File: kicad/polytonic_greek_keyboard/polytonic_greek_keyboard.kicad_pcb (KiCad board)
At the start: 2 copper layers, 10 parts, among them SW1 SW_Wuerth_450301014042, SW2 RotaryEncoder_Switch_MP, SW3 SW_SPST, SW4 SW_SP4T_NR01104, U1 ESP32-S2-WROVER

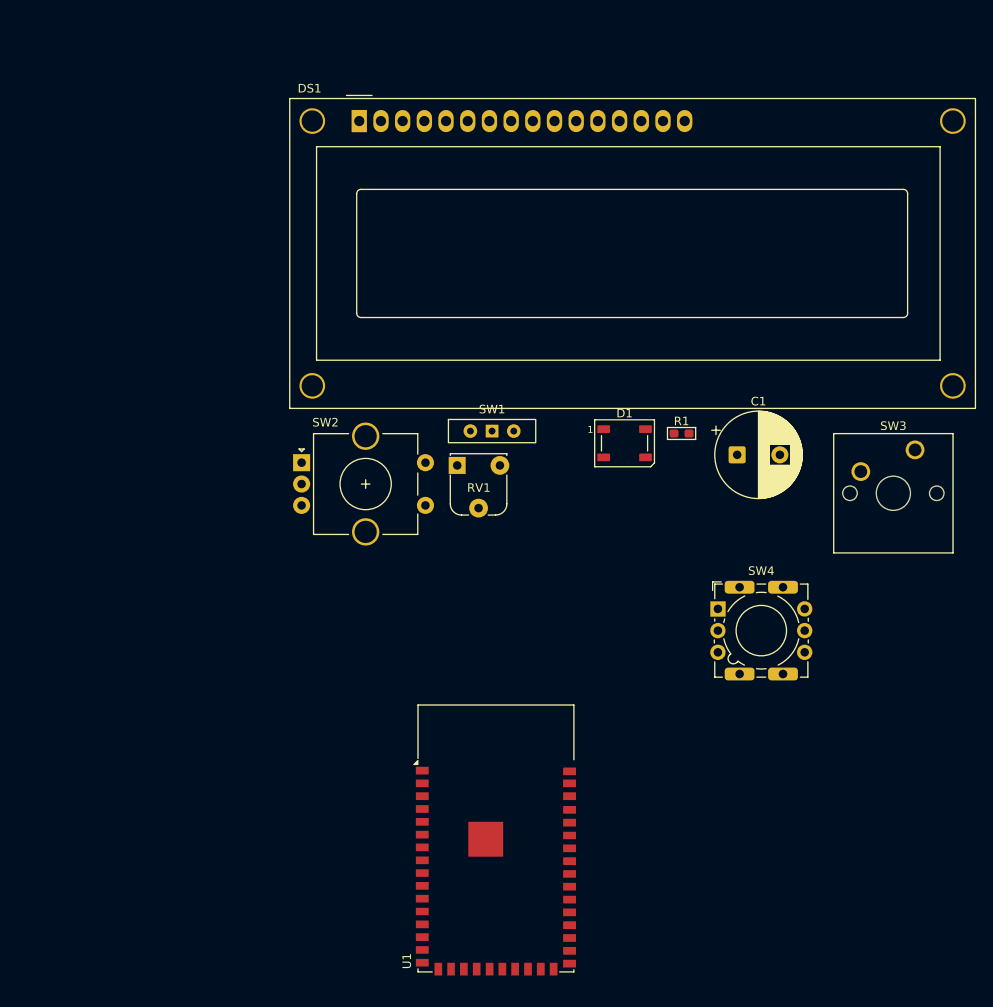
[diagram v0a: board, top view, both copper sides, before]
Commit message: [ADD] the kicad desing of the I²C chip for the keybard
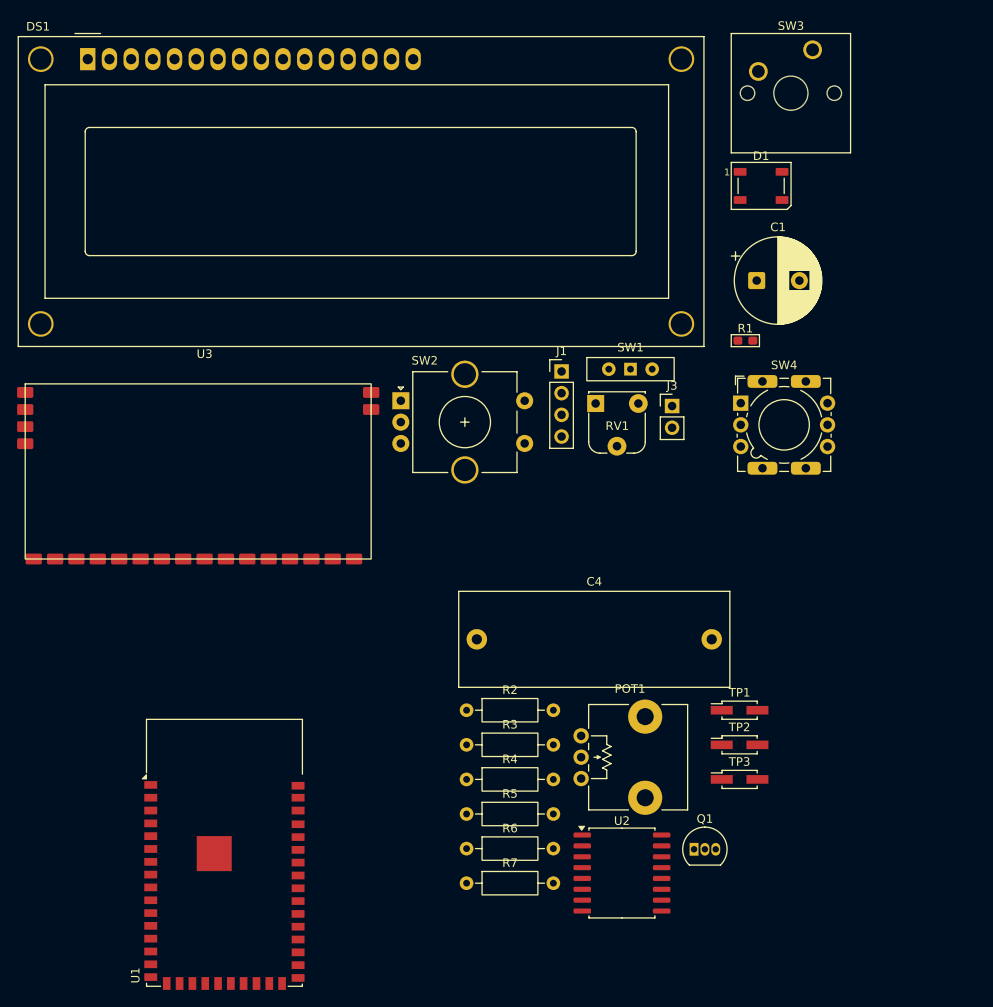
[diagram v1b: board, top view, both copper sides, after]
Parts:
- added C4: 0.1uF, Capacitor_THT:C_Rect_L31.5mm_W11.0mm_P27.50mm_MKS4, F.Cu at (85.2, 94.6)
- added J1: PINHD_1x4_Male, Connector_PinHeader_2.54mm:PinHeader_1x04_P2.54mm_Vertical, F.Cu at (95.1, 63.2)
- added J3: PINHD_1x2_Male, Connector_PinHeader_2.54mm:PinHeader_1x02_P2.54mm_Vertical, F.Cu at (108.0, 67.3)
- added POT1: 16mm_CtrDet_10k, PCM_Potentiometer_THT_US_AKL:Potentiometer_Alps_RK09L_Single_Vertical, F.Cu at (97.4, 110.9)
- added Q1: S8050, Package_TO_SOT_THT:TO-92_Inline, F.Cu at (110.6, 119.2)
- added R2: 47k, Resistor_THT:R_Axial_DIN0207_L6.3mm_D2.5mm_P10.16mm_Horizontal, F.Cu at (84.0, 102.9)
- added R3: 1k, Resistor_THT:R_Axial_DIN0207_L6.3mm_D2.5mm_P10.16mm_Horizontal, F.Cu at (84.0, 107.0)
- added R4: 1k, Resistor_THT:R_Axial_DIN0207_L6.3mm_D2.5mm_P10.16mm_Horizontal, F.Cu at (84.0, 111.0)
- added R5: 1k, Resistor_THT:R_Axial_DIN0207_L6.3mm_D2.5mm_P10.16mm_Horizontal, F.Cu at (84.0, 115.0)
- added R6: 47k, Resistor_THT:R_Axial_DIN0207_L6.3mm_D2.5mm_P10.16mm_Horizontal, F.Cu at (84.0, 119.1)
- added R7: 47k, Resistor_THT:R_Axial_DIN0207_L6.3mm_D2.5mm_P10.16mm_Horizontal, F.Cu at (84.0, 123.2)
- added TP1: TestPoint_2Pole, Pin_Headers:Pin_Header_Straight_2x01_Pitch2.00mm_SMD, F.Cu at (115.9, 102.9)
- added TP2: TestPoint_2Pole, Pin_Headers:Pin_Header_Straight_2x01_Pitch2.00mm_SMD, F.Cu at (115.9, 107.0)
- added TP3: TestPoint_2Pole, Pin_Headers:Pin_Header_Straight_2x01_Pitch2.00mm_SMD, F.Cu at (115.9, 111.0)
- added U2: PCF8574T, Package_SO:SOIC-16W_7.5x10.3mm_P1.27mm, F.Cu at (102.1, 122.0)
- added U3: ~, polytonic_greek_keyboard:I²C, F.Cu at (53.3, 61.7)
- moved SW3 48.4 mm to (124.5, 25.6)
- moved D1 34.1 mm to (118.4, 41.5)
- moved DS1 32.6 mm to (39.6, 26.7)
- moved U1 31.8 mm to (55.6, 123.4)
- moved SW4 24.2 mm to (116.1, 67.0)
- moved C1 20.5 mm to (117.9, 52.6)
- moved RV1 17.8 mm to (101.6, 69.0)
- moved SW1 17.8 mm to (103.1, 63.0)
- moved SW2 13.7 mm to (76.3, 66.7)
- moved R1 13.2 mm to (116.6, 59.6)
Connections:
- net /display/VDD_SCREEN renamed /display/VCC_SCREEN
- DS1 pad 1: VSS -> Net-(DS1-VSS)
- DS1 pad 11: unconnected-(DS1-D4-Pad11) -> Net-(DS1-D4)
- DS1 pad 12: unconnected-(DS1-D5-Pad12) -> Net-(DS1-D5)
- DS1 pad 13: unconnected-(DS1-D6-Pad13) -> Net-(DS1-D6)
- DS1 pad 14: unconnected-(DS1-D7-Pad14) -> Net-(DS1-D7)
- DS1 pad 16: GND -> Net-(DS1-LED(-))
- DS1 pad 3: unconnected-(DS1-VO-Pad3) -> Net-(DS1-VO)
- DS1 pad 4: unconnected-(DS1-RS-Pad4) -> Net-(DS1-RS)
- DS1 pad 5: unconnected-(DS1-R/W-Pad5) -> Net-(DS1-R/W)
- DS1 pad 6: unconnected-(DS1-E-Pad6) -> Net-(DS1-E)
- RV1 pad 1: Net-(DS1-LED(+)) -> Net-(U3-LED_VCC)
- RV1 pad 3: Net-(DS1-VDD) -> Net-(SW1-C)
- SW1 pad 2: Net-(DS1-VDD) -> Net-(SW1-C)

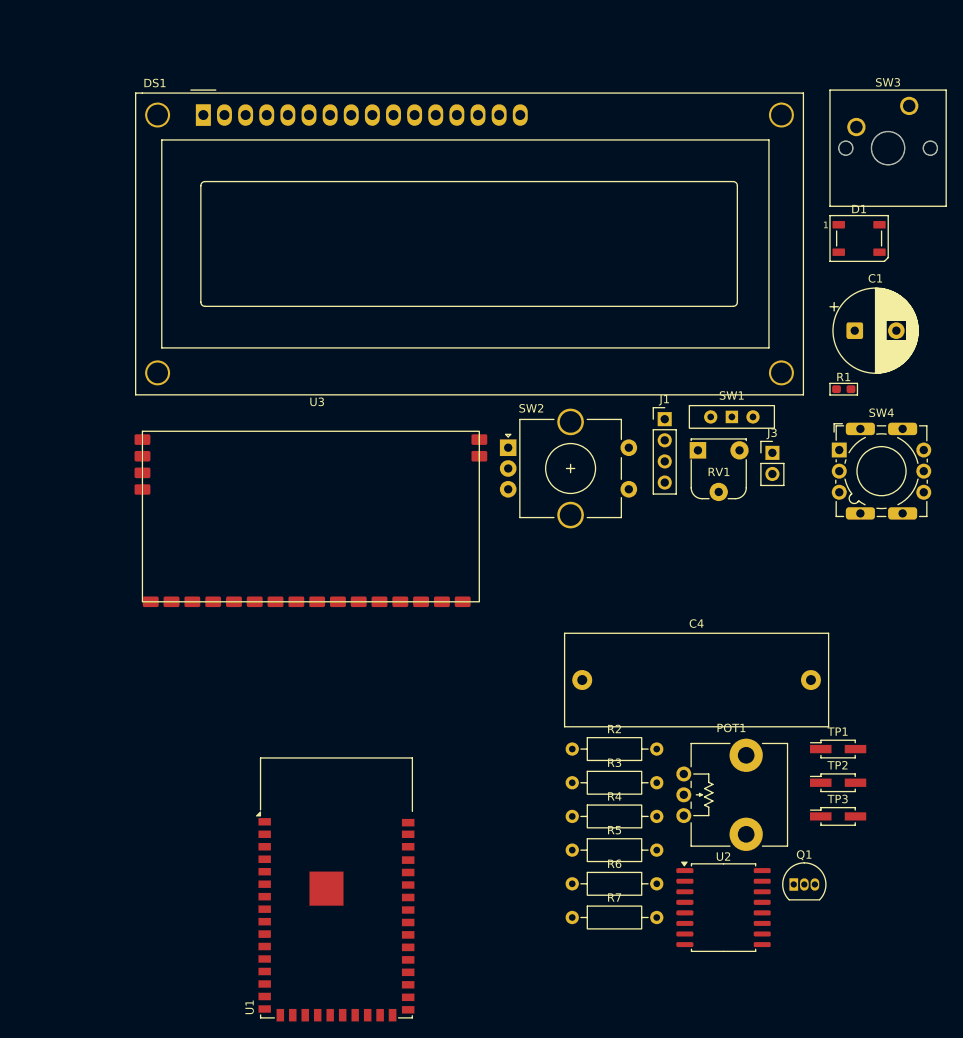
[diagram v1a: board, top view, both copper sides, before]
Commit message: [ADD] an initial matrix of what the keyboard will look like logically
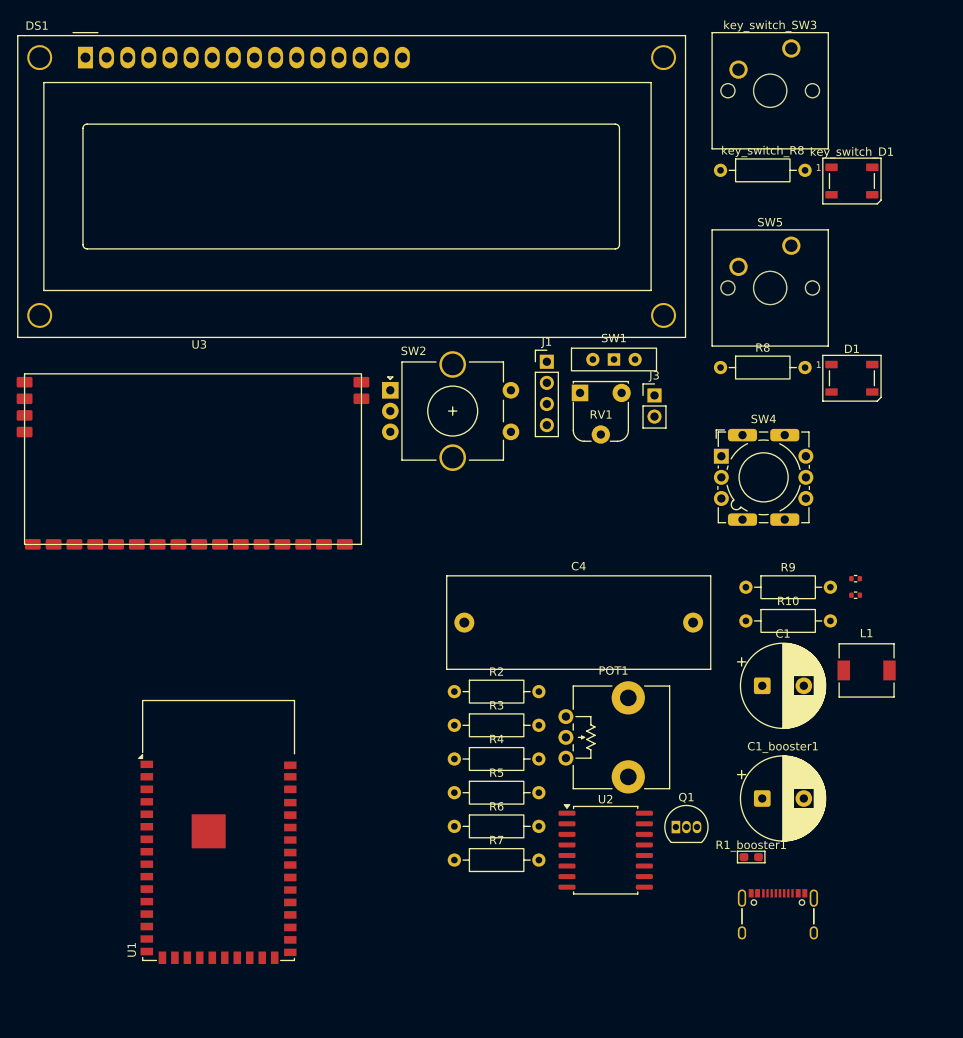
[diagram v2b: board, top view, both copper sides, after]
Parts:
- removed R1: 330R_0603, PCM_Resistor_SMD_AKL:R_0603_1608Metric_Pad1.05x0.95mm_HandSolder
- removed SW3: SW_SPST, Button_Switch_Keyboard:SW_Cherry_MX_1.00u_PCB
- removed TP1, TP2, TP3: TestPoint_2Pole, Pin_Headers:Pin_Header_Straight_2x01_Pitch2.00mm_SMD
- added C1_booster1: 1000uF_16V, Capacitor_THT:CP_Radial_D10.0mm_P5.00mm, F.Cu at (106.8, 108.8)
- added J2: USB_C_Receptacle, PCM_SparkFun-Connector:USB-C_16, F.Cu at (108.7, 119.9)
- added L1: FerriteBead_0603_1.5A, Inductor_SMD:L_6.3x6.3_H3, F.Cu at (119.3, 93.4)
- added R10: 22ohm, Resistor_THT:R_Axial_DIN0207_L6.3mm_D2.5mm_P10.16mm_Horizontal, F.Cu at (104.8, 87.5)
- added R11: 5.1k, PCM_SparkFun-Resistor:R_0402_1005Metric, F.Cu at (118.0, 82.4)
- added R12: 5.1k, PCM_SparkFun-Resistor:R_0402_1005Metric, F.Cu at (118.0, 84.4)
- added R1_booster1: 330R_0603, PCM_Resistor_SMD_AKL:R_0603_1608Metric_Pad1.05x0.95mm_HandSolder, F.Cu at (105.5, 115.9)
- added R8: 330ohm, Resistor_THT:R_Axial_DIN0207_L6.3mm_D2.5mm_P10.16mm_Horizontal, F.Cu at (101.8, 57.0)
- added R9: 22ohm, Resistor_THT:R_Axial_DIN0207_L6.3mm_D2.5mm_P10.16mm_Horizontal, F.Cu at (104.8, 83.4)
- added SW5: SW_SPST, Button_Switch_Keyboard:SW_Cherry_MX_1.00u_PCB, F.Cu at (110.3, 42.4)
- added key_switch_D1: WS2812B, LED_SMD:LED_WS2812B_PLCC4_5.0x5.0mm_P3.2mm, F.Cu at (117.6, 34.6)
- added key_switch_R8: 330ohm, Resistor_THT:R_Axial_DIN0207_L6.3mm_D2.5mm_P10.16mm_Horizontal, F.Cu at (101.8, 33.3)
- added key_switch_SW3: SW_SPST, Button_Switch_Keyboard:SW_Cherry_MX_1.00u_PCB, F.Cu at (110.3, 18.7)
- moved C1 44.1 mm to (106.8, 95.3)
- moved D1 16.8 mm to (117.6, 58.3)
- moved J3 15.8 mm to (93.8, 60.4)
- moved C4 15.8 mm to (71.0, 87.7)
- moved J1 15.8 mm to (80.9, 56.3)
- moved POT1 15.8 mm to (83.2, 104.0)
- moved R2 15.8 mm to (69.8, 96.0)
- moved R3 15.8 mm to (69.8, 100.0)
- moved R4 15.8 mm to (69.8, 104.1)
- moved R5 15.8 mm to (69.8, 108.1)
- moved R6 15.8 mm to (69.8, 112.2)
- moved R7 15.8 mm to (69.8, 116.2)
- moved SW1 15.8 mm to (89.0, 56.1)
- moved U3 15.8 mm to (39.1, 54.8)
- moved RV1 15.8 mm to (87.4, 62.1)
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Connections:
- net /key_switch/LED_DOUT renamed /key_alpha/LED_DOUT
- net /key_switch/VDD_led renamed Net-(D1-VDD)
- net VSS renamed /key_alpha/LED_VSS
- C1 pad 1: /5v_led_booster/VDD -> /power_filter/GND_IN
- C1 pad 2: Net-(C1-Pad2) -> /power_filter/VBUS_OUT
- D1 pad 4: /key_switch/LED_DIN -> Net-(D1-DIN)
